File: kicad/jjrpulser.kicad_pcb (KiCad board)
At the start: 2 copper layers, 55.9 x 44.7 mm, 18 parts, among them J1 3.3V, J2 3.3V, J3 Screw_Terminal_HOT, J4 Screw_Terminal_COLD, J5 Conn_UART, U1 ESP-12

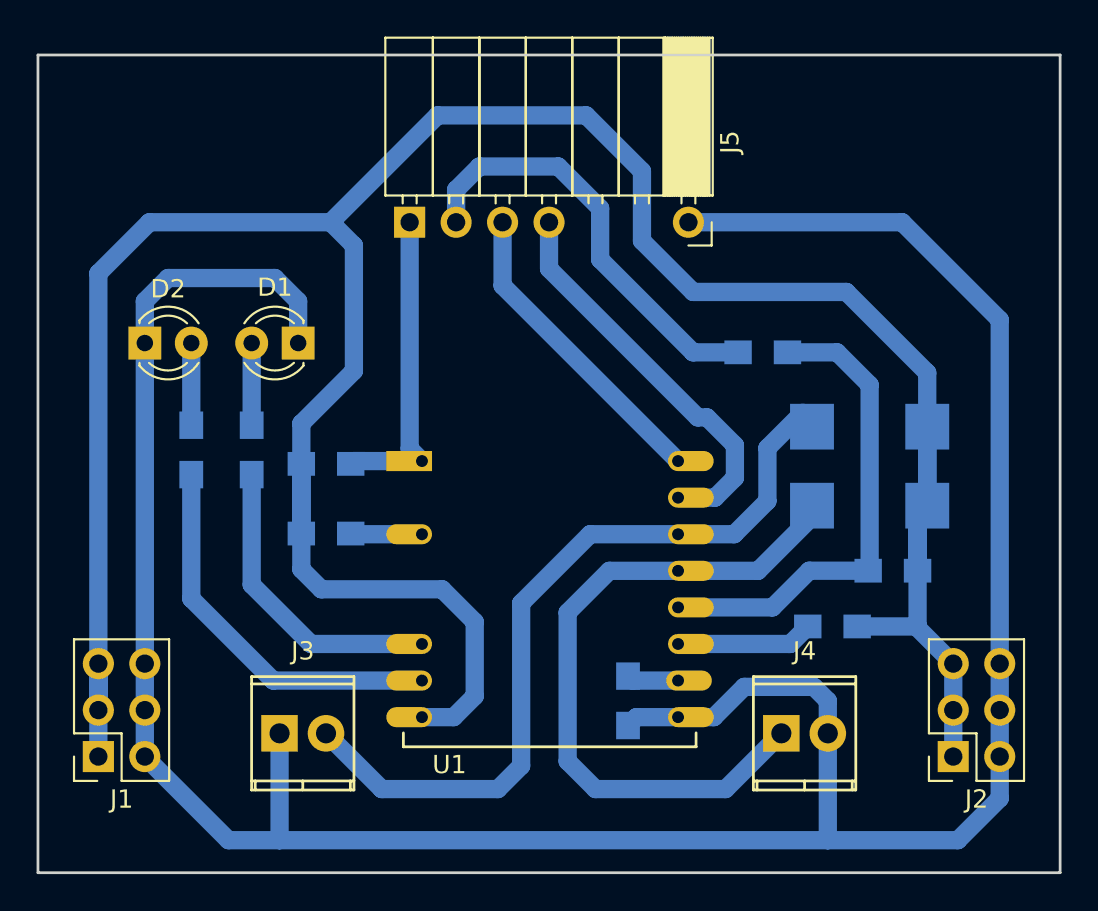
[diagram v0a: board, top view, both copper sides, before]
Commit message: Расстояние между ножками блока питания уменьшено до 47мм
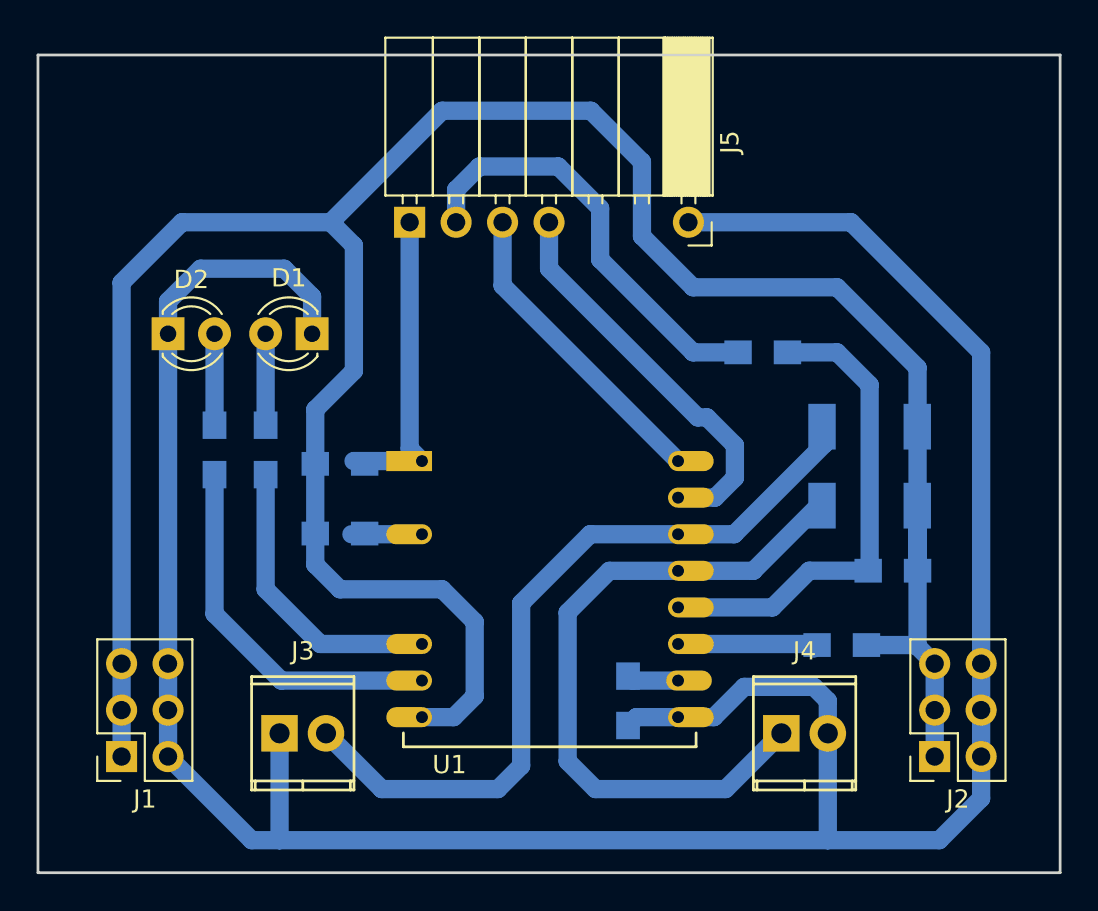
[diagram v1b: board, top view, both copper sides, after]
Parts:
- R10, R5: footprint Resistors_SMD:R_2010_HandSoldering -> Resistors_SMD:R_2010
- moved D2 1.37 mm to (134.6, 98.0)
- moved J1 1.27 mm to (132.1, 121.2)
- moved R4 1.27 mm to (137.2, 104.4)
- moved R7 1.14 mm to (171.4, 115.1)
- moved J2 1.02 mm to (176.5, 121.2)
- moved D1 0.92 mm to (142.5, 98.0)
- moved R1 0.76 mm to (140.0, 104.4)
- moved R2 0.76 mm to (144.0, 105.2)
- moved R3 0.76 mm to (144.0, 109.0)
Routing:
- net +3V3: track 161.9 -> 147.3 mm
- net Earth: track 157.2 -> 152.4 mm
- net Net-(J4-Pad1): track 37.0 -> 38.0 mm
- net Net-(R4-Pad2): track 21.2 -> 20.5 mm
- net Net-(R1-Pad2): track 16.7 -> 16.1 mm
- net Net-(D2-Pad2): track 4.49 -> 5.00 mm
- net Net-(D1-Pad2): track 4.49 -> 5.00 mm

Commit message: Мелкие улучшения трассировки
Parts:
- moved D1 0.76 mm to (142.5, 98.8)
- moved D2 0.76 mm to (134.6, 98.8)
- moved R2 0.15 mm to (144.0, 105.0)
- moved R7 0.05 mm to (171.4, 115.0)
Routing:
- net +3V3: track 147.3 -> 145.6 mm
- net Earth: track 152.4 -> 153.6 mm
- net Net-(J5-Pad4): track 22.0 -> 23.0 mm
- net Net-(D2-Pad2): track 5.00 -> 4.24 mm
- net Net-(D1-Pad2): track 5.00 -> 4.24 mm
- net Net-(R3-Pad1): track 3.86 -> 3.13 mm
- net Net-(J5-Pad1): track 17.1 -> 16.5 mm
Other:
- board size 55.9 x 44.7 mm -> 51.1 x 44.7 mm

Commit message: Еще немного гламура в трассировку
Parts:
- moved R6 0.13 mm to (159.8, 118.0)
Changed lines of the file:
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@@
     (links 42)
     (no_connects 0)
-    (area 129.972999 81.272999 181.177001 127.583001)
+    (area 129.972999 82.728999 181.177001 127.583001)
     (thickness 1.6)
     (drawings 8)
-    (tracks 116)
+    (tracks 118)
     (zones 0)
     (modules 18)
@@
   )
   (module Resistors_SMD:R_0805_HandSoldering (layer B.Cu)
-    (at 159.766 118.11 90)
+    (at 159.766 117.983 90)
     (descr "Resistor SMD 0805, hand soldering")
     (tags "resistor 0805")
@@
   (gr_line (start 181.102 82.804) (end 181.102 127.508) (angle 90) (layer Edge.Cuts) (width 0.15))
   (gr_line (start 130.048 127.508) (end 130.048 82.804) (angle 90) (layer Edge.Cuts) (width 0.15))
+  (segment (start 162.5011 119.0036) (end 161.18586 119.0036) (width 1) (layer B.Cu) (net 1) (status 400000))
+  (segment (start 160.85646 119.333) (end 159.766 119.333) (width 1) (layer B.Cu) (net 1) (status 800000))
+  (segment (start 161.18586 119.0036) (end 160.85646 119.333) (width 1) (layer B.Cu) (net 1))
   (segment (start 134.62 116.078) (end 134.62 98.806) (width 1) (layer B.Cu) (net 1) (status 30))
   (segment (start 134.62 98.806) (end 134.62 96.266) (width 1) (layer B.Cu) (net 1) (status 10))
@@
   (segment (start 179.07 118.618) (end 179.07 121.158) (width 1) (layer B.Cu) (net 1) (status 30))
   (segment (start 170.688 125.73) (end 140.716 125.73) (width 1) (layer B.Cu) (net 1))
-  (segment (start 162.5011 119.0036) (end 160.2224 119.0036) (width 1) (layer B.Cu) (net 1) (status 30))
-  (segment (start 160.2224 119.0036) (end 159.766 119.46) (width 1) (layer B.Cu) (net 1) (status 30))
   (segment (start 139.954 98.806) (end 139.954 103.044) (width 1) (layer B.Cu) (net 2) (status 30))
   (segment (start 137.16 98.806) (end 137.16 103.044) (width 1) (layer B.Cu) (net 3) (status 30))
@@
   (segment (start 151.384 117.856) (end 151.384 113.792) (width 1) (layer B.Cu) (net 4))
   (segment (start 150.2364 119.0036) (end 151.384 117.856) (width 1) (layer B.Cu) (net 4))
-  (segment (start 162.5011 117.0036) (end 160.0096 117.0036) (width 1) (layer B.Cu) (net 5) (status 30))
-  (segment (start 160.0096 117.0036) (end 159.766 116.76) (width 1) (layer B.Cu) (net 5) (status 30))
+  (segment (start 162.5011 117.0036) (end 161.23896 117.0036) (width 1) (layer B.Cu) (net 5) (status 400000))
+  (segment (start 160.86836 116.633) (end 159.766 116.633) (width 1) (layer B.Cu) (net 5) (status 800000))
+  (segment (start 161.23896 117.0036) (end 160.86836 116.633) (width 1) (layer B.Cu) (net 5))
   (segment (start 162.5011 115.0036) (end 170.0924 115.0036) (width 1) (layer B.Cu) (net 6))
   (segment (start 162.5011 113.0036) (end 167.6664 113.0036) (width 1) (layer B.Cu) (net 7) (status 10))
